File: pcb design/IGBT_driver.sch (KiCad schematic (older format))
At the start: 52 parts, among them J2 DESAT, Q13 NPN, Q14 PNP, U1 ISO5852S, U6 NAND, U8 TLP2745

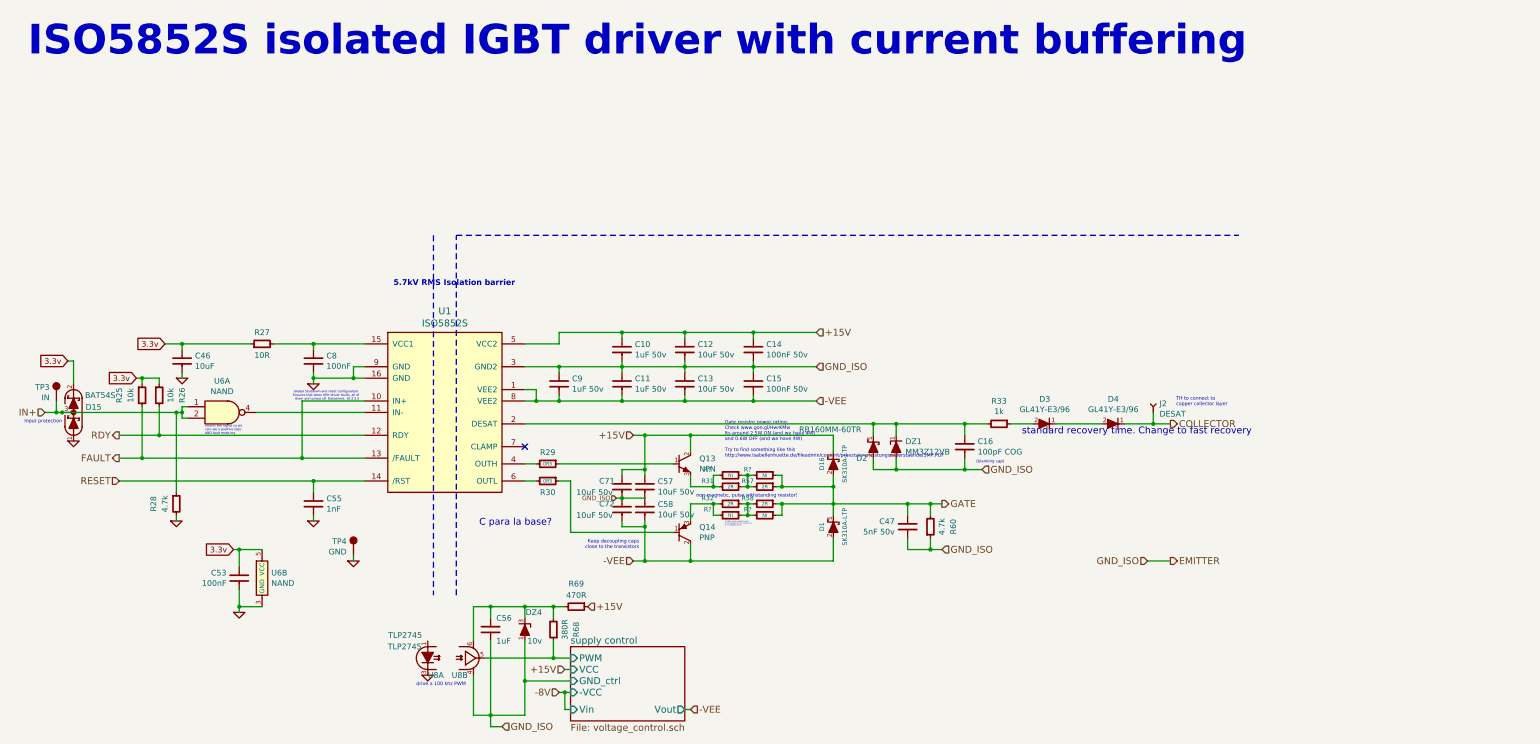
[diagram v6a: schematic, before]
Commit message: Added comments before I forget things, changed X5R to X7R. Updated PCB
Signed-off-by: Marcos Chaparro <mchaparro@paltatech.com>
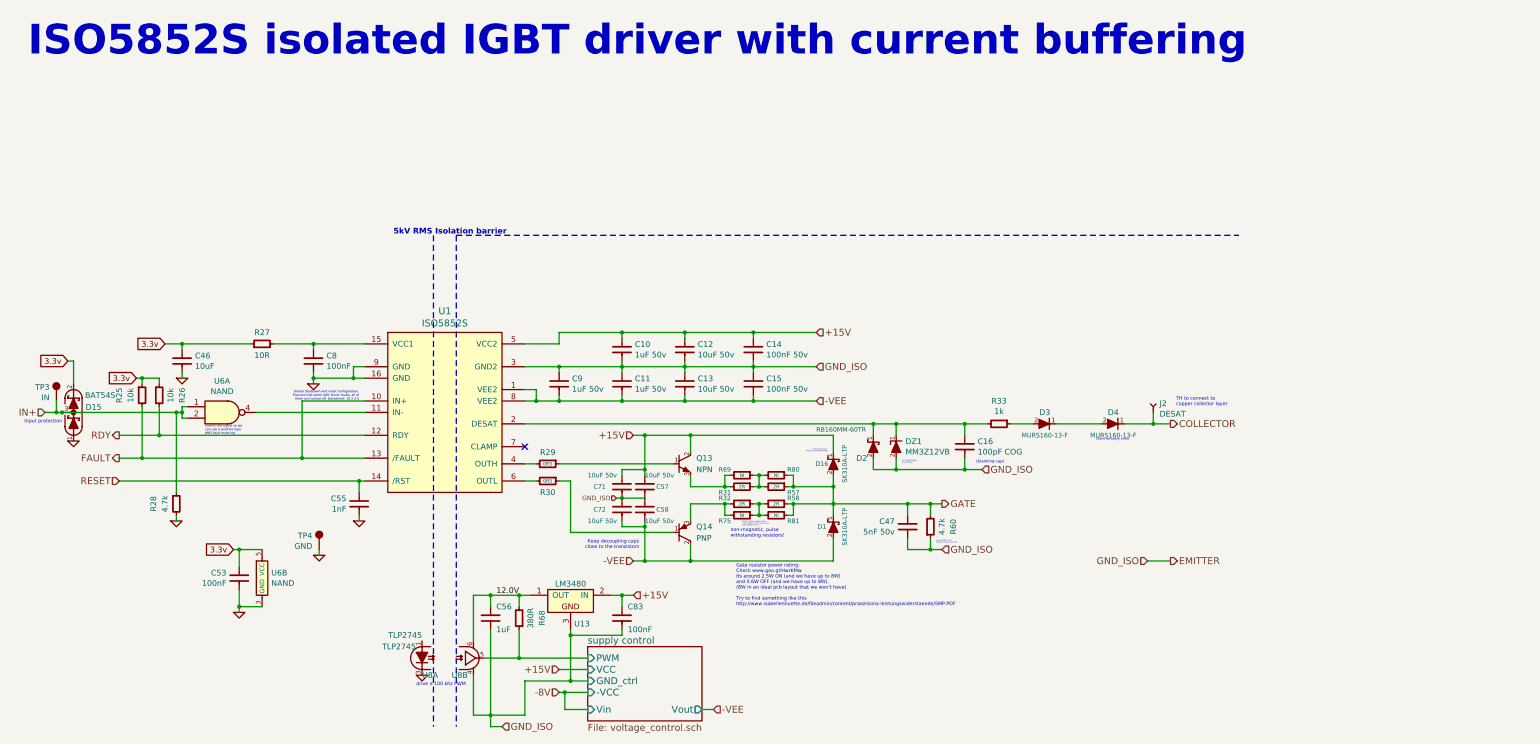
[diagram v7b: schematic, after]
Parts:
- removed DZ4: 10v, smd-semi:SOT-23, symbol BZX84
- removed R69: 470R, IPC7351-Nominal:RESC1608X50, symbol R-0603
- added C83: 100nF, IPC7351-Nominal:CAPC1608X55, symbol C-0603
- added U13: LM3480, smd-semi:SOT-23, symbol LM3480
- C12, C13, C57, C58, C71, C72: mfg# CL31A106KBHNNNE -> CL31B106KBHNNNE
- D3, D4: value GL41Y-E3/96 -> MURS160-13-F
- R31, R32, R57, R58: footprint IPC7351-Nominal:RESC3225X60 -> IPC7351-Nominal:RESC3216X60
- R69, R75, R80, R81: renamed from R?; footprint IPC7351-Nominal:RESC3225X60 -> IPC7351-Nominal:RESC3216X60
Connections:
- net +15V: now also C83.1, U13.2 (IN)
- net EMITTER: now also C83.2, U13.3
- net 12.0V: now reaches C56.1, R68.2, U8.6 (VCC)
- net 12.0V: now also U13.1 (OUT)
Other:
- note added: "(50ns recovery time)"
- note added: "12V 200mW zener\nfor protection"
- note added: "5kV RMS Isolation barrier"
- note added: "Ensures IGBT is OFF\nwhile driver is powered off"
- note added: "Gate resistor power rating:\nCheck www.goo.gl/HwrKMw\nIts around 2.5W ON (and we have up to 8W)\nand 0.6W OFF (and we have up to 8W).\n(8W in an ideal pcb layout that we won't have)\n\nTry to find something like this\nhttp://www.isabellenhuette.de/fileadmin/content/praezisions-leistungswiderstaende/SMP.PDF"
- note added: "Latchup protection.\nA latchup here blows IGBTs"
- note added: "non-magnetic, pulse\nwithstanding resistors!"
- note removed: "5.7kV RMS Isolation barrier"
- note removed: "C para la base?"
- note removed: "Gate resistor power rating:\nCheck www.goo.gl/HwrKMw\nIts around 2.5W ON (and we have 4W)\nand 0.6W OFF (and we have 4W)\n\nTry to find something like this\nhttp://www.isabellenhuette.de/fileadmin/content/praezisions-leistungswiderstaende/SMP.PDF"
- note removed: "non-magnetic, pulse withstanding resistor!"
- note removed: "standard recovery time. Change to fast recovery"
- moved on the sheet: C55, C56, R31, R32, R57, R58, R68, R69, R75, R80, R81, TP4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

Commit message: Power supply sync input. And more comments
Signed-off-by: Marcos Chaparro <mchaparro@paltatech.com>
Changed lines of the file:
@@
 (50ns recovery time)
 Wire Wire Line
-	4950 3900 5250 3900
-Wire Wire Line
-	5250 3900 5800 3900
-Wire Wire Line
-	5800 3900 6350 3900
-Wire Wire Line
-	6350 3900 6950 3900
-Wire Wire Line
-	6950 3900 7500 3900
-Wire Wire Line
-	5800 3850 5800 3900
-Wire Wire Line
-	5800 3900 5800 3950
+	4950 3900 7500 3900
+Wire Wire Line
+	5800 3850 5800 3950
 Connection ~ 5800 3900
 Wire Wire Line
-	6350 3850 6350 3900
-Wire Wire Line
-	6350 3900 6350 3950
+	6350 3850 6350 3950
 Connection ~ 6350 3900
 Wire Wire Line
-	6950 3850 6950 3900
-Wire Wire Line
-	6950 3900 6950 3950
+	6950 3850 6950 3950
 Connection ~ 6950 3900
 Wire Wire Line
 	6950 3600 6950 3650
 Wire Wire Line
-	5250 3600 5800 3600
-Wire Wire Line
-	5800 3600 6350 3600
-Wire Wire Line
-	6350 3600 6950 3600
-Wire Wire Line
-	6950 3600 7500 3600
+	5250 3600 7500 3600
 Wire Wire Line
 	6350 3600 6350 3650
@@
 Connection ~ 5800 3600
 Wire Wire Line
-	4950 4200 5050 4200
-Wire Wire Line
-	5050 4200 5250 4200
-Wire Wire Line
-	5250 4200 5800 4200
-Wire Wire Line
-	5800 4200 6350 4200
-Wire Wire Line
-	6350 4200 6950 4200
-Wire Wire Line
-	6950 4200 7500 4200
+	4950 4200 7500 4200
 Wire Wire Line
 	5250 4200 5250 4150
@@
 	3550 3900 3450 3900
 Wire Wire Line
-	3100 4000 3450 4000
-Wire Wire Line
-	3450 4000 3550 4000
+	3100 4000 3550 4000
 Wire Wire Line
 	3450 3900 3450 4000
 Wire Wire Line
-	3100 3950 3100 4000
-Wire Wire Line
-	3100 4000 3100 4050
+	3100 3950 3100 4050
 Connection ~ 3450 4000
 Connection ~ 3100 4000
@@
 	3100 3750 3100 3700
 Wire Wire Line
-	2750 3700 3100 3700
-Wire Wire Line
-	3100 3700 3550 3700
+	2750 3700 3550 3700
 Connection ~ 3100 3700
 Wire Wire Line
-	1800 3700 1950 3700
-Wire Wire Line
-	1950 3700 2550 3700
+	1800 3700 2550 3700
 Wire Wire Line
 	4950 4900 5050 4900
@@
 	4950 4750 5050 4750
 Wire Wire Line
-	6400 4950 6700 4950
-Wire Wire Line
-	6700 4950 6750 4950
+	6400 4950 6750 4950
 Wire Wire Line
 	6400 4850 6400 4950
@@
 	6400 5100 6400 5250
 Wire Wire Line
-	6400 5100 6700 5100
-Wire Wire Line
-	6700 5100 6750 5100
+	6400 5100 6750 5100
 Wire Wire Line
 	5250 4750 6250 4750
@@
 	5350 4900 5250 4900
 Wire Wire Line
-	6950 4950 7000 4950
-Wire Wire Line
-	7000 4950 7050 4950
-Wire Wire Line
-	6950 5100 7000 5100
-Wire Wire Line
-	7000 5100 7050 5100
-Wire Wire Line
-	7250 5100 7300 5100
-Wire Wire Line
-	7300 5100 7650 5100
-Wire Wire Line
-	7650 5100 8300 5100
-Wire Wire Line
-	8300 5100 8500 5100
-Wire Wire Line
-	8500 5100 8600 5100
-Wire Wire Line
-	7650 4850 7650 4950
-Wire Wire Line
-	7650 4950 7650 5100
-Wire Wire Line
-	7650 5100 7650 5200
-Wire Wire Line
-	7250 4950 7300 4950
-Wire Wire Line
-	7300 4950 7650 4950
+	6950 4950 7050 4950
+Wire Wire Line
+	6950 5100 7050 5100
+Wire Wire Line
+	7250 5100 8600 5100
+Wire Wire Line
+	7650 4850 7650 5200
+Wire Wire Line
+	7250 4950 7650 4950
 Wire Wire Line
 	6400 5600 6400 5450
 Wire Wire Line
-	5900 5600 6000 5600
-Wire Wire Line
-	6000 5600 6400 5600
-Wire Wire Line
-	6400 5600 7650 5600
+	5900 5600 7650 5600
 Wire Wire Line
 	6400 4500 6400 4650
 Wire Wire Line
-	5900 4500 6000 4500
-Wire Wire Line
-	6000 4500 6400 4500
-Wire Wire Line
-	6400 4500 7650 4500
-Wire Wire Line
-	1400 4700 1600 4700
-Wire Wire Line
-	1600 4700 3000 4700
-Wire Wire Line
-	3000 4700 3550 4700
+	5900 4500 7650 4500
+Wire Wire Line
+	1400 4700 3550 4700
 Wire Wire Line
 	1600 4700 1600 4250
 Wire Wire Line
-	1550 4000 1600 4000
-Wire Wire Line
-	1600 4000 1750 4000
+	1550 4000 1750 4000
 Wire Wire Line
 	1600 4000 1600 4050
@@
 	1750 4250 1750 4500
 Wire Wire Line
-	1400 4500 1750 4500
-Wire Wire Line
-	1750 4500 3550 4500
+	1400 4500 3550 4500
 Wire Wire Line
 	1750 4000 1750 4050
 Connection ~ 1600 4000
 Wire Wire Line
-	4950 4400 8000 4400
-Wire Wire Line
-	8000 4400 8200 4400
-Wire Wire Line
-	8200 4400 8800 4400
-Wire Wire Line
-	8800 4400 9000 4400
+	4950 4400 9000 4400
 Wire Wire Line
 	8800 4400 8800 4500
@@
 	8000 4700 8000 4800
 Wire Wire Line
-	8000 4800 8200 4800
-Wire Wire Line
-	8200 4800 8800 4800
-Wire Wire Line
-	8800 4800 8950 4800
+	8000 4800 8950 4800
 Wire Wire Line
 	8200 4800 8200 4700
@@
 Connection ~ 8800 4800
 Wire Wire Line
-	10200 4400 10450 4400
-Wire Wire Line
-	10450 4400 10600 4400
+	10200 4400 10600 4400
 Wire Wire Line
 	10400 5600 10600 5600
@@
 Connection ~ 1600 4700
 Wire Wire Line
-	1400 4900 3500 4900
-Wire Wire Line
-	3500 4900 3550 4900
+	1400 4900 3550 4900
 Wire Wire Line
 	8300 5200 8300 5100
 Connection ~ 8300 5100
 Wire Wire Line
-	8300 5500 8500 5500
-Wire Wire Line
-	8500 5500 8600 5500
+	8300 5500 8600 5500
 Wire Wire Line
 	8300 5500 8300 5400
@@
 Connection ~ 10450 4400
 Wire Wire Line
-	750  4300 850  4300
-Wire Wire Line
-	850  4300 900  4300
-Wire Wire Line
-	900  4300 1900 4300
-Wire Wire Line
-	1900 4300 1950 4300
+	750  4300 1950 4300
 Connection ~ 900  4300
 Wire Wire Line
@@
 Connection ~ 850  4300
 Wire Wire Line
-	2400 5500 2450 5500
-Wire Wire Line
-	2450 5500 2650 5500
+	2400 5500 2650 5500
 Wire Wire Line
 	2450 5500 2450 5650
@@
 	2650 6000 2450 6000
 Wire Wire Line
-	2450 5850 2450 6000
-Wire Wire Line
-	2450 6000 2450 6050
+	2450 5850 2450 6050
 Connection ~ 2450 6000
 Connection ~ 2450 5500
@@
 	3500 5250 3500 5200
 Wire Wire Line
-	4600 6450 4900 6450
-Wire Wire Line
-	4900 6450 5500 6450
+	4600 6450 5500 6450
 Wire Wire Line
 	4500 5900 4500 6300
 Wire Wire Line
-	4500 5900 4650 5900
-Wire Wire Line
-	4650 5900 4900 5900
-Wire Wire Line
-	4900 5900 5000 5900
+	4500 5900 5000 5900
 Wire Wire Line
 	4650 5900 4650 6000
 Wire Wire Line
-	4650 6200 4650 6950
-Wire Wire Line
-	4650 6950 4650 7050
+	4650 6200 4650 7050
 Wire Wire Line
 	4900 5900 4900 6000
@@
 	4900 6450 4900 6200
 Wire Wire Line
-	4500 6950 4650 6950
-Wire Wire Line
-	4650 6950 4950 6950
+	4500 6950 4950 6950
 Wire Wire Line
 	4950 6950 4950 6650
 Wire Wire Line
-	6000 5250 6000 5300
-Wire Wire Line
-	6000 5300 6000 5600
+	6000 5250 6000 5600
 Connection ~ 6000 5600
 Wire Wire Line
-	6000 4500 6000 4800
-Wire Wire Line
-	6000 4800 6000 4850
+	6000 4500 6000 4850
 Connection ~ 6000 4500
 Wire Wire Line
-	5750 5050 5800 5050
-Wire Wire Line
-	5800 5050 6000 5050
+	5750 5050 6000 5050
 Connection ~ 4900 6450
 Connection ~ 5800 5050
@@
 	4650 7050 4750 7050
 Wire Wire Line
-	4950 6650 5350 6650
-Wire Wire Line
-	5350 6650 5500 6650
+	4950 6650 5500 6650
 Wire Wire Line
 	5250 6550 5500 6550
 Wire Wire Line
-	5250 6750 5300 6750
-Wire Wire Line
-	5300 6750 5500 6750
+	5250 6750 5500 6750
 Wire Wire Line
 	5300 6750 5300 6900
@@
 Connection ~ 1900 4300
 Wire Wire Line
-	1950 4250 1950 4300
-Wire Wire Line
-	1950 4300 1950 4350
+	1950 4250 1950 4350
 Wire Wire Line
 	1950 4350 2000 4350
@@
 	3000 4200 3000 4700
 Wire Wire Line
-	6950 5200 7000 5200
-Wire Wire Line
-	7000 5200 7050 5200
+	6950 5200 7050 5200
 Wire Wire Line
 	7000 5200 7000 5100
@@
 Connection ~ 7000 5200
 Wire Wire Line
-	6950 4850 7000 4850
-Wire Wire Line
-	7000 4850 7050 4850
+	6950 4850 7050 4850
 Wire Wire Line
 	7000 4850 7000 4950
@@
 Connection ~ 4650 5900
 Wire Wire Line
-	5700 5900 5800 5900
-Wire Wire Line
-	5800 5900 5900 5900
+	5700 5900 5900 5900
 Wire Wire Line
 	5800 6000 5800 5900
@@
 	5800 6250 5350 6250
 Wire Wire Line
-	5350 6200 5350 6250
-Wire Wire Line
-	5350 6250 5350 6650
+	5350 6200 5350 6650
 Connection ~ 5350 6250
 Connection ~ 5350 6650
